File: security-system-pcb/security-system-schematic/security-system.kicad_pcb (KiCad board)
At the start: 4 copper layers, 102 x 41 mm, 9 parts, among them J1 TF-LUNA-CONNECTOR, J2 POWER USB_C, U1 ESP32-Header

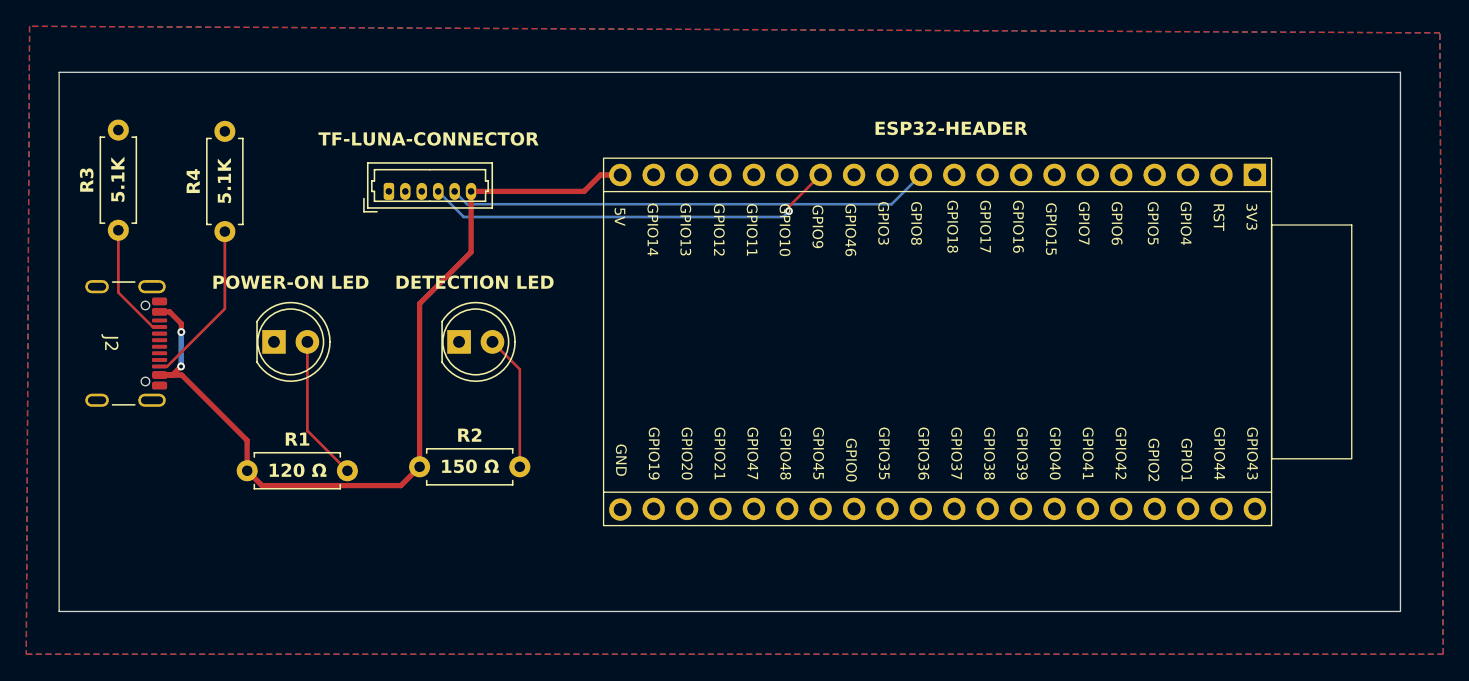
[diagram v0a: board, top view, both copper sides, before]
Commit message: Add PCB changes and 3D case
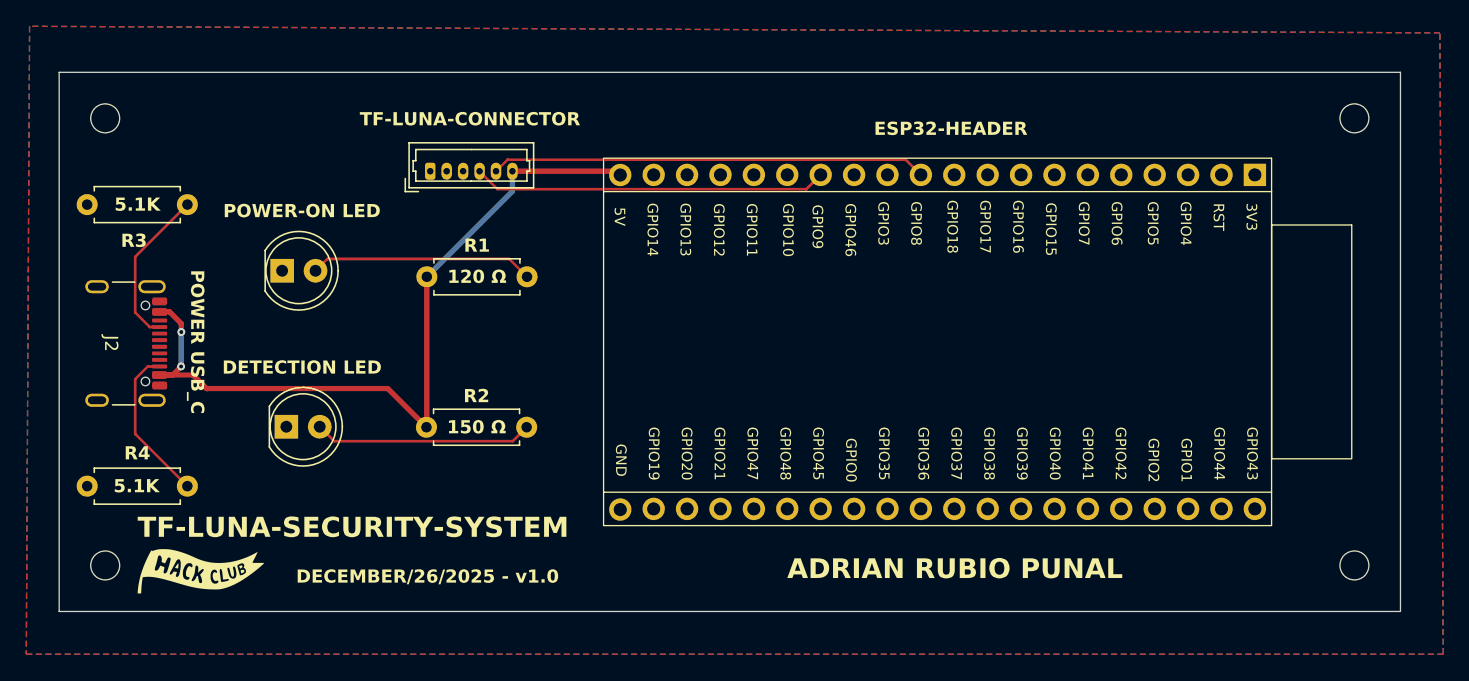
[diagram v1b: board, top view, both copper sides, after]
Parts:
- added G***: LOGO, LOGO, F.Cu at (135.8, 103.9)
- added G***: LOGO, LOGO, B.Cu at (135.8, 103.9)
- moved R1 20.1 mm to (153.0, 81.5)
- moved R4 19.6 mm to (134.8, 97.5), turned to 180 degrees
- moved DETECTION LED 14.6 mm to (142.3, 93.0)
- moved R3 5.60 mm to (134.8, 76.1), turned to 180 degrees
- moved POWER-ON LED 5.45 mm to (142.0, 81.1)
- moved J1 3.50 mm to (153.2, 73.5)
- moved R2 3.05 mm to (152.9, 93.0)
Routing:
- net +5V: track 66.9 -> 59.6 mm
- net Net-(D2-A): track 10.4 -> 16.6 mm
- net Net-(D1-A): track 11.1 -> 17.0 mm
- net /SCL: track 31.4 -> 27.0 mm, vias 1 -> 0
- net /SDA: track 36.8 -> 33.2 mm
- net Net-(J2-CC1): track 8.95 -> 12.2 mm
- net Net-(J2-CC2): track 12.7 -> 12.0 mm
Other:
- outline, holes or cut-outs redrawn
- board text added: "ADRIAN RUBIO PUNAL"
- board text added: "DECEMBER/26/2025 - v1.0"
- board text added: "TF-LUNA-SECURITY-SYSTEM"

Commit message: Add updated gerbers
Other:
- board text added: "DECEMBER/26/2025 - v1.1"
- board text removed: "DECEMBER/26/2025 - v1.0"
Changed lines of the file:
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@@
 			(drillshape 0)
 			(scaleselection 1)
-			(outputdirectory "gerbers/")
+			(outputdirectory "gerbers/security-system-v1.1/")
 		)
 	)
@@
 		)
 	)
-	(gr_text "DECEMBER/26/2025 - v1.0"
+	(gr_text "DECEMBER/26/2025 - v1.1"
 		(at 153.012311 104.93 0)
 		(layer "F.SilkS")

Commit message: Push PCB version 1.3
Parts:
- D1: renamed from POWER-ON LED
- D2: renamed from DETECTION LED
- J1: value TF-LUNA-CONNECTOR -> Conn_01x06_Pin
- J2: value POWER USB_C -> USB_C
- R2: value 150 Ω -> 60 Ω
- moved U1 1.95 mm to (204.2, 86.5)
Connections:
- R2 pad 1: +5V -> /LED_STATUS
- U1 pad 5: unconnected-(U1-GPIO4-Pad5) -> /LED_STATUS
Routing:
- net /LED_STATUS: track 0.00 -> 67.8 mm
- net +5V: track 59.6 -> 49.6 mm
- net /SDA: track 33.2 -> 35.2 mm
- net /SCL: track 27.0 -> 28.7 mm
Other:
- board text added: "DECEMBER/26/2025 - v1.3"
- board text removed: "DECEMBER/26/2025 - v1.1"
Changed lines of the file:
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@@
 			(drillshape 0)
 			(scaleselection 1)
-			(outputdirectory "gerbers/security-system-v1.1/")
+			(outputdirectory "gerbers/security-system-v1.2/")
 		)
 	)
@@
 	(net 22 "unconnected-(U1-GPIO38-Pad18)")
 	(net 23 "unconnected-(U1-GPIO21-Pad34)")
-	(net 24 "unconnected-(U1-GPIO4-Pad5)")
+	(net 24 "/LED_STATUS")
 	(net 25 "unconnected-(U1-GPIO47-Pad32)")
 	(net 26 "unconnected-(U1-GPIO41-Pad12)")
@@
 		(descr "LED, diameter 5.0mm, 2 pins, http://cdn-reichelt.de/documents/datenblatt/A500/LL-504BC2E-009.pdf, generated by kicad-footprint-generator")
 		(tags "LED")
-		(property "Reference" "DETECTION LED"
+		(property "Reference" "D2"
 			(at 1.19 -4.5 0)
 			(layer "F.SilkS")
@@
 		(descr "LED, diameter 5.0mm, 2 pins, http://cdn-reichelt.de/documents/datenblatt/A500/LL-504BC2E-009.pdf, generated by kicad-footprint-generator")
 		(tags "LED")
-		(property "Reference" "POWER-ON LED"
+		(property "Reference" "D1"
 			(at 1.505 -4.54 0)
 			(layer "F.SilkS")
@@
 			)
 		)
-		(property "Value" "TF-LUNA-CONNECTOR"
+		(property "Value" "Conn_01x06_Pin"
 			(at 3.025 -3.955 0)
 			(layer "F.SilkS")
@@
 			)
 		)
-		(property "Value" "POWER USB_C"
-			(at -0.12 -6.545 270)
+		(property "Value" "USB_C"
+			(at -0.12 -8.045 270)
 			(unlocked yes)
 			(layer "F.SilkS")
@@
 			)
 		)
-		(property "Datasheet" ""
+		(property "Datasheet" "https://www.usb.org/sites/default/files/documents/usb_type-c.zip"
 			(at 0 0 270)
 			(unlocked yes)
@@
 			)
 		)
-		(property "Description" ""
+		(property "Description" "USB 2.0-only 16P Type-C Receptacle connector"
 			(at 0 0 270)
 			(unlocked yes)
@@
 	(footprint "security-system-footprints:esp32-header"
 		(layer "F.Cu")
-		(at 202.25 86.5 -90)
+		(at 204.202 86.5 -90)
 		(property "Reference" "U1"
 			(at -11.95 38.47 270)
@@
 			(layers "*.Cu" "*.Mask")
 			(remove_unused_layers no)
-			(net 24 "unconnected-(U1-GPIO4-Pad5)")
+			(net 24 "/LED_STATUS")
 			(pinfunction "GPIO4")
-			(pintype "passive+no_connect")
+			(pintype "passive")
 		)
 		(pad "6" thru_hole circle
@@
 			(polygon
 				(pts
-					(xy 217.2 72.5) (xy 217.2 100.5) (xy 166.4475 100.5) (xy 166.4475 72.5)
+					(xy 219.152 72.5) (xy 219.152 100.5) (xy 168.3995 100.5) (xy 168.3995 72.5)
 				)
 			)
@@
 			)
 		)
-		(property "Value" "150 Ω"
+		(property "Value" "60 Ω"
 			(at 3.81 0 0)
 			(layer "F.SilkS")
@@
 			(layers "*.Cu" "*.Mask")
 			(remove_unused_layers no)
-			(net 4 "+5V")
+			(net 24 "/LED_STATUS")
 			(pintype "passive")
 		)
@@
 		)
 	)
-	(gr_text "DECEMBER/26/2025 - v1.1"
+	(gr_text "DECEMBER/26/2025 - v1.3"
 		(at 153.012311 104.93 0)
 		(layer "F.SilkS")
@@
 	)
 	(segment
-		(start 167.38 73.52)
-		(end 167.67 73.81)
-		(width 0.4)
-		(layer "F.Cu")
-		(net 4)
-	)
-	(segment
 		(start 132.635 89.02)
 		(end 133.62 89.02)
@@
 	)
 	(segment
-		(start 136.21 90.05)
-		(end 135.18 89.02)
+		(start 152.96 81.55)
+		(end 150.29 84.22)
 		(width 0.4)
 		(layer "F.Cu")
@@
 	)
 	(segment
-		(start 152.96 81.55)
-		(end 152.96 92.96)
-		(width 0.4)
-		(layer "F.Cu")
-		(net 4)
-	)
-	(segment
-		(start 149.99 90.05)
-		(end 136.21 90.05)
-		(width 0.4)
-		(layer "F.Cu")
-		(net 4)
-	)
-	(segment
 		(start 134.29 85.75)
 		(end 134.29 85.11)
@@
 	)
 	(segment
-		(start 135.18 89.02)
-		(end 132.635 89.02)
+		(start 150.29 84.22)
+		(end 132.635 84.22)
 		(width 0.4)
 		(layer "F.Cu")
@@
 	(segment
 		(start 159.47 73.52)
-		(end 167.38 73.52)
+		(end 169.332 73.52)
 		(width 0.4)
 		(layer "F.Cu")
@@
 	)
 	(segment
-		(start 152.96 92.96)
-		(end 152.93 92.99)
+		(start 169.332 73.52)
+		(end 169.622 73.81)
 		(width 0.4)
 		(layer "F.Cu")
@@
 		(net 4)
 	)
-	(segment
-		(start 152.93 92.99)
-		(end 149.99 90.05)
-		(width 0.4)
-		(layer "F.Cu")
-		(net 4)
-	)
 	(via
 		(at 134.29 85.75)
@@
 	(segment
 		(start 156.97 73.52)
-		(end 158.338 74.888)
-		(width 0.2)
+		(end 157.8115 72.6785)
+		(width 0.127)
 		(layer "F.Cu")
 		(net 5)
 	)
 	(segment
-		(start 158.338 74.888)
-		(end 181.822 74.888)
-		(width 0.2)
+		(start 183.7405 72.6785)
+		(end 184.862 73.8)
+		(width 0.127)
 		(layer "F.Cu")
 		(net 5)
 	)
 	(segment
-		(start 181.822 74.888)
-		(end 182.91 73.8)
-		(width 0.2)
+		(start 157.8115 72.6785)
+		(end 183.7405 72.6785)
+		(width 0.127)
 		(layer "F.Cu")
 		(net 5)
@@
 	(segment
 		(start 158.22 73.52)
-		(end 159.098 72.642)
-		(width 0.2)
+		(end 159.5515 74.8515)
+		(width 0.127)
 		(layer "F.Cu")
 		(net 6)
 	)
 	(segment
-		(start 159.098 72.642)
-		(end 189.372 72.642)
-		(width 0.2)
+		(start 191.4305 74.8515)
+		(end 192.482 73.8)
+		(width 0.127)
 		(layer "F.Cu")
 		(net 6)
 	)
 	(segment
-		(start 189.372 72.642)
-		(end 190.53 73.8)
-		(width 0.2)
+		(start 159.5515 74.8515)
+		(end 191.4305 74.8515)
+		(width 0.127)
 		(layer "F.Cu")
 		(net 6)
@@
 		(net 13)
 	)
+	(segment
+		(start 159.52 86.4)
+		(end 200.202 86.4)
+		(width 0.2)
+		(layer "F.Cu")
+		(net 24)
+	)
+	(segment
+		(start 200.202 86.4)
+		(end 212.802 73.8)
+		(width 0.2)
+		(layer "F.Cu")
+		(net 24)
+	)
+	(segment
+		(start 152.93 92.99)
+		(end 159.52 86.4)
+		(width 0.2)
+		(layer "F.Cu")
+		(net 24)
+	)
 	(zone
